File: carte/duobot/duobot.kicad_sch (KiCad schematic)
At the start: 28 parts, among them J1 Conn_01x08, J2 Conn_01x10, J3 Conn_01x02, J4 Conn_01x06, J5 Conn_01x04, J6 Conn_01x04, X1 Trou, X2 Trou, X3 Trou, X4 Trou

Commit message: Finalisation routage et schéma
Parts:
- removed J1: Conn_01x08, symbol Connector_Generic:Conn_01x08
- added U1: ~, bpc:BPC_MPU6050, symbol bpc:BPC_MPU6050
- C1: value C_Polarized -> 20µF
- C2: value C -> 1nF
- C3, C4: value C_Polarized -> 100µF
- C5, C6: value C -> 100nF
- J2: value Conn_01x10 -> Extension; footprint (none) -> Connector_PinHeader_2.54mm:PinHeader_2x05_P2.54mm_Vertical; symbol Connector_Generic:Conn_01x10 -> Connector_Generic:Conn_02x05_Odd_Even
- J3: value Conn_01x02 -> Alimentation
- J4: value Conn_01x06 -> HC05 - BT; footprint (none) -> Connector_PinHeader_2.54mm:PinHeader_1x06_P2.54mm_Vertical
- J5: value Conn_01x04 -> Moteur Gauche
- J6: value Conn_01x04 -> Moteur Droite
- R1, R2: value R -> 10k
- R3, R4: value R -> 100k
- R5, R6, R7, R8: value R -> 0
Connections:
- net +5V: now also J2.10 (Pin_10), U1.1 (Vcc); no longer J2.9 (Pin_9)
- net A0: now also J2.4 (Pin_4); no longer J2.3 (Pin_3)
- net A1: now also J2.6 (Pin_6); no longer J2.4 (Pin_4)
- net A2: now also J2.8 (Pin_8); no longer J2.5 (Pin_5)
- net A3: now also J2.7 (Pin_7); no longer J2.6 (Pin_6)
- net A6: now also J2.5 (Pin_5); no longer J2.7 (Pin_7)
- net A7: now also J2.3 (Pin_3); no longer J2.8 (Pin_8)
- net GND: now also J2.9 (Pin_9), U1.2 (Gnd); no longer J2.10 (Pin_10)
- net SCL: now also U1.3 (SCL)
- net SDA: now also U1.4 (SDA)
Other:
- note added: "NM"
- company: BPC -> Paul
- moved on the sheet: J2, R1, R2

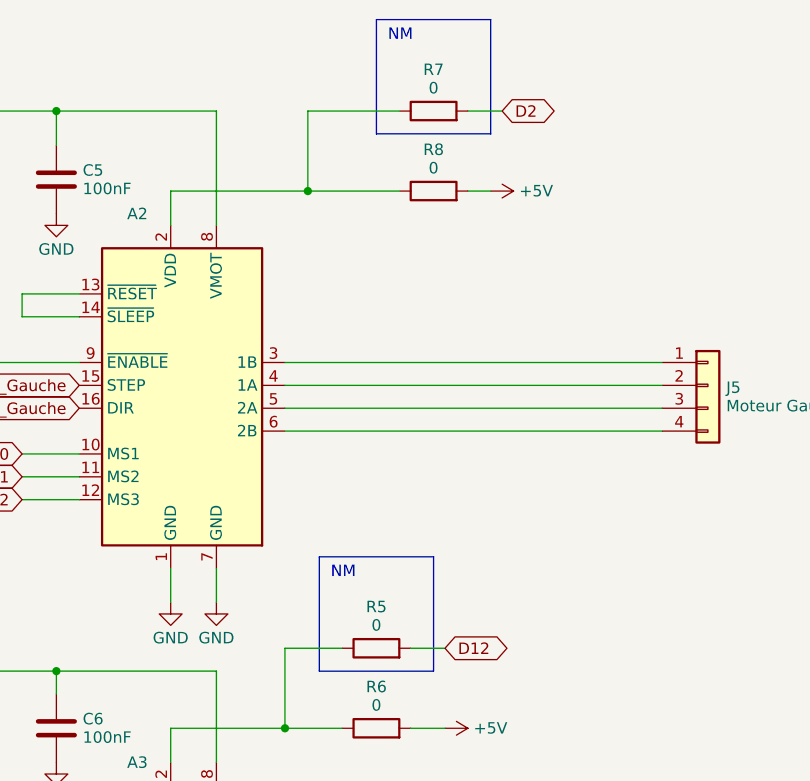
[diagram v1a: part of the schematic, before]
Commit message: Carte: Petite correction référence R5 et R8 sur le schéma Création du programme de test de la carte: OK
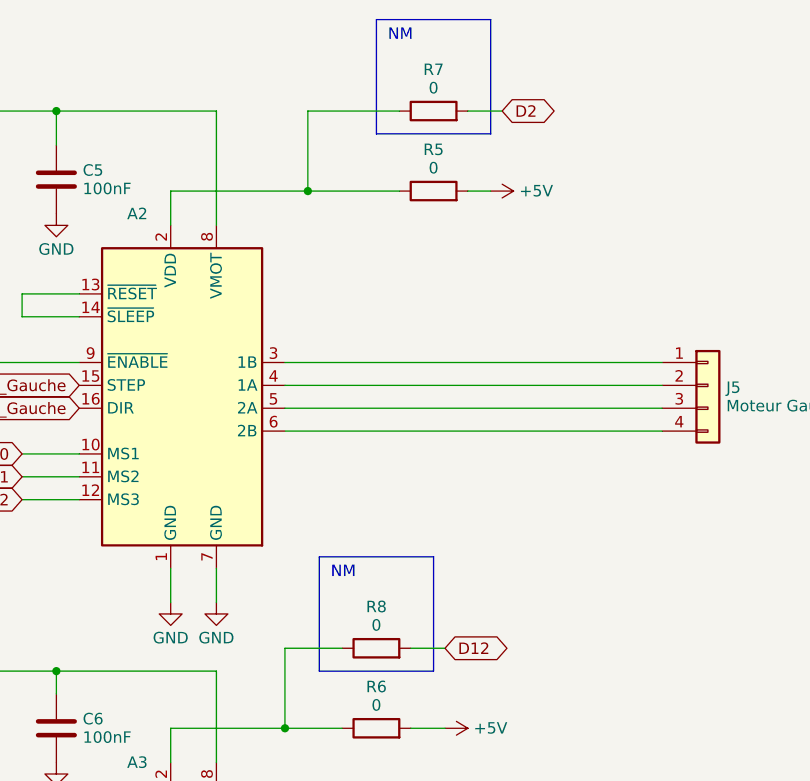
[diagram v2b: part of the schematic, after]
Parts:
- renumbered R8 to R5, R5 to R8
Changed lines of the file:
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@@
   (symbol (lib_id "Device:R") (at 236.22 36.83 90) (unit 1)
     (in_bom yes) (on_board yes) (dnp no) (fields_autoplaced)
-    (property "Reference" "R8" (at 236.22 32.234 90)
+    (property "Reference" "R5" (at 236.22 32.234 90)
       (effects (font (size 1.27 1.27)))
     )
@@
       (project "duobot"
         (path "/bbb811a8-250b-4b92-a455-cbc7c5328174"
-          (reference "R8") (unit 1)
+          (reference "R5") (unit 1)
         )
       )
@@
   (symbol (lib_id "Device:R") (at 229.87 87.63 90) (unit 1)
     (in_bom yes) (on_board yes) (dnp no) (fields_autoplaced)
-    (property "Reference" "R5" (at 229.87 83.034 90)
+    (property "Reference" "R8" (at 229.87 83.034 90)
       (effects (font (size 1.27 1.27)))
     )
@@
       (project "duobot"
         (path "/bbb811a8-250b-4b92-a455-cbc7c5328174"
-          (reference "R5") (unit 1)
-        )
-      )
+          (reference "R8") (unit 1)
+        )
+      )
